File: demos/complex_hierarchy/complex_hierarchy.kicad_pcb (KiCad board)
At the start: 2 copper layers, 100.7 x 80 mm, 68 parts, among them P1 CONN_2, P2 CONN_2, P3 CONN_2, P4 CONN_2, P5 CONN_2, P6 CONN_2, Q1 MPSA92, Q2 MPSA42, Q3 MPSA92, Q4 MPSA42, Q5 MPSA92, Q6 MPSA42, Q7 MPSA92, Q8 MPSA42, U1 ICL7660, U2 78L05, U3 LM358N, U4 LM358N

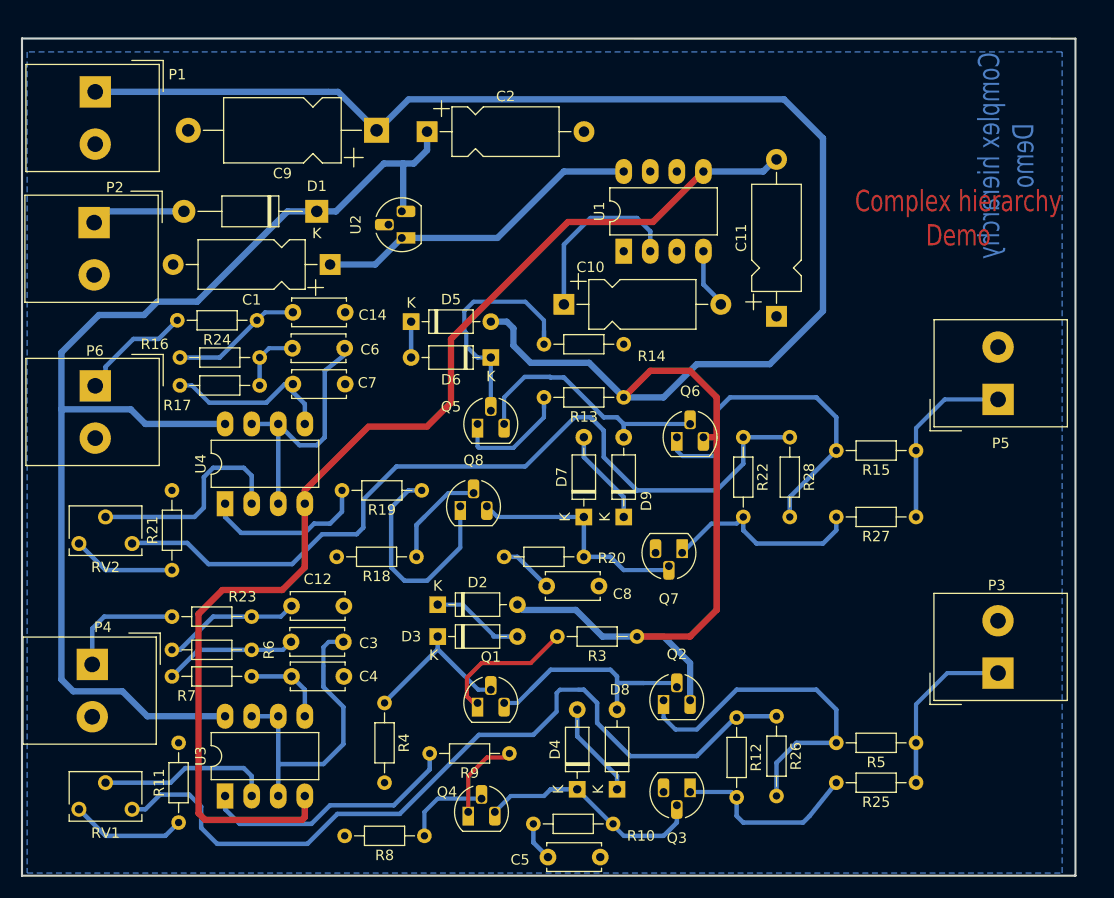
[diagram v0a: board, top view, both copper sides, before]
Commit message: feat: update kicad to 9.0.0+dfsg-1
Signed-off-by: lhdjply <lhdjply@126.com>
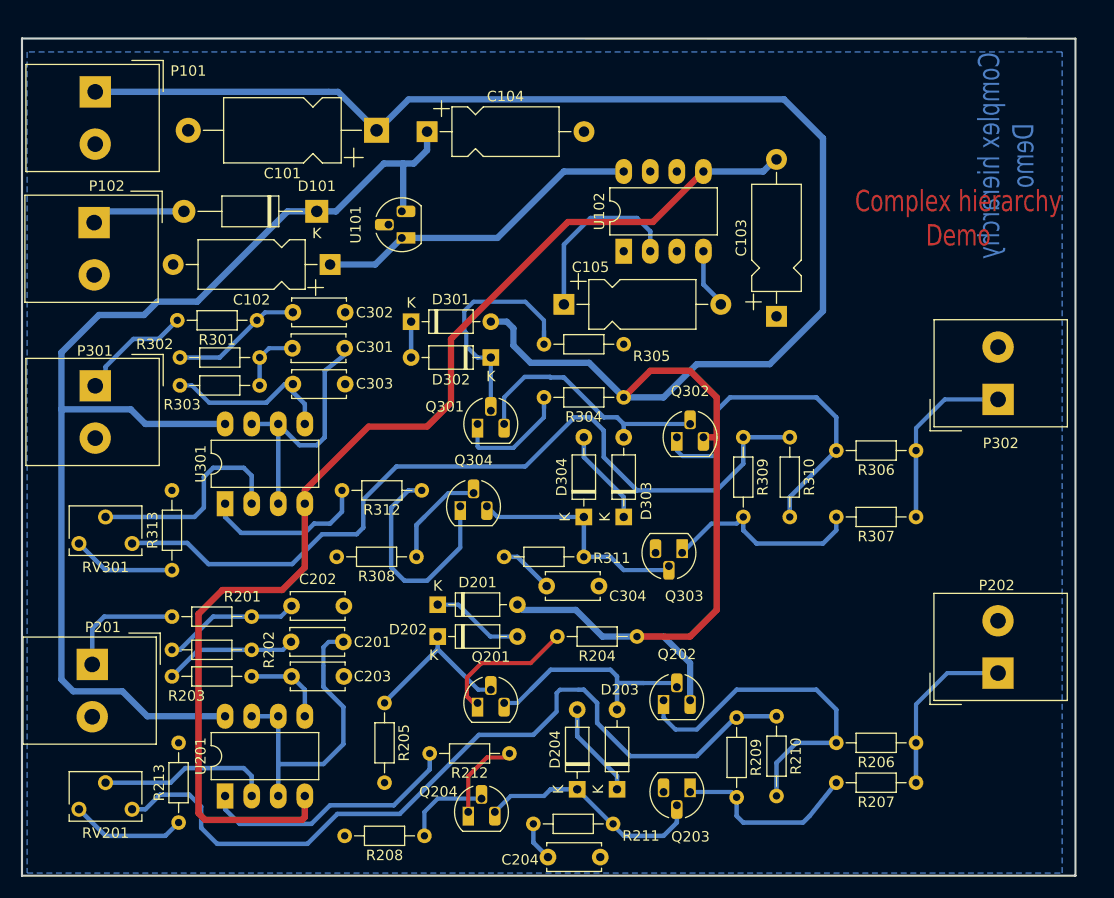
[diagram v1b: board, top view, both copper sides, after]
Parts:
- C101: renamed from C9; footprint Capacitor_THT:CP_Axial_L11.0mm_D6.0mm_P18.00mm_Horizontal -> complex_hierarchy:CP_Axial_L11.0mm_D6.0mm_P18.00mm_Horizontal
- C102: renamed from C1; footprint Capacitor_THT:CP_Axial_L10.0mm_D4.5mm_P15.00mm_Horizontal -> complex_hierarchy:CP_Axial_L10.0mm_D4.5mm_P15.00mm_Horizontal
- C103: renamed from C11; footprint Capacitor_THT:CP_Axial_L10.0mm_D4.5mm_P15.00mm_Horizontal -> complex_hierarchy:CP_Axial_L10.0mm_D4.5mm_P15.00mm_Horizontal
- C104: renamed from C2; footprint Capacitor_THT:CP_Axial_L10.0mm_D4.5mm_P15.00mm_Horizontal -> complex_hierarchy:CP_Axial_L10.0mm_D4.5mm_P15.00mm_Horizontal
- C105: renamed from C10; footprint Capacitor_THT:CP_Axial_L10.0mm_D4.5mm_P15.00mm_Horizontal -> complex_hierarchy:CP_Axial_L10.0mm_D4.5mm_P15.00mm_Horizontal
- C201: renamed from C3; footprint Capacitor_THT:C_Disc_D5.0mm_W2.5mm_P5.00mm -> complex_hierarchy:C_Disc_D5.0mm_W2.5mm_P5.00mm
- C202: renamed from C12; footprint Capacitor_THT:C_Disc_D5.0mm_W2.5mm_P5.00mm -> complex_hierarchy:C_Disc_D5.0mm_W2.5mm_P5.00mm
- C203: renamed from C4; footprint Capacitor_THT:C_Disc_D5.0mm_W2.5mm_P5.00mm -> complex_hierarchy:C_Disc_D5.0mm_W2.5mm_P5.00mm
- C204: renamed from C5; footprint Capacitor_THT:C_Disc_D5.0mm_W2.5mm_P5.00mm -> complex_hierarchy:C_Disc_D5.0mm_W2.5mm_P5.00mm
- C301: renamed from C6; footprint Capacitor_THT:C_Disc_D5.0mm_W2.5mm_P5.00mm -> complex_hierarchy:C_Disc_D5.0mm_W2.5mm_P5.00mm
- C302: renamed from C14; footprint Capacitor_THT:C_Disc_D5.0mm_W2.5mm_P5.00mm -> complex_hierarchy:C_Disc_D5.0mm_W2.5mm_P5.00mm
- C303: renamed from C7; footprint Capacitor_THT:C_Disc_D5.0mm_W2.5mm_P5.00mm -> complex_hierarchy:C_Disc_D5.0mm_W2.5mm_P5.00mm
- C304: renamed from C8; footprint Capacitor_THT:C_Disc_D5.0mm_W2.5mm_P5.00mm -> complex_hierarchy:C_Disc_D5.0mm_W2.5mm_P5.00mm
- D101: renamed from D1; footprint Diode_THT:D_DO-41_SOD81_P12.70mm_Horizontal -> complex_hierarchy:D_DO-41_SOD81_P12.70mm_Horizontal
- D201: renamed from D2; footprint Diode_THT:D_DO-35_SOD27_P7.62mm_Horizontal -> complex_hierarchy:D_DO-35_SOD27_P7.62mm_Horizontal
- D202: renamed from D3; footprint Diode_THT:D_DO-35_SOD27_P7.62mm_Horizontal -> complex_hierarchy:D_DO-35_SOD27_P7.62mm_Horizontal
- D203: renamed from D8; footprint Diode_THT:D_DO-35_SOD27_P7.62mm_Horizontal -> complex_hierarchy:D_DO-35_SOD27_P7.62mm_Horizontal
- D204: renamed from D4; footprint Diode_THT:D_DO-35_SOD27_P7.62mm_Horizontal -> complex_hierarchy:D_DO-35_SOD27_P7.62mm_Horizontal
- D301: renamed from D5; footprint Diode_THT:D_DO-35_SOD27_P7.62mm_Horizontal -> complex_hierarchy:D_DO-35_SOD27_P7.62mm_Horizontal
- D302: renamed from D6; footprint Diode_THT:D_DO-35_SOD27_P7.62mm_Horizontal -> complex_hierarchy:D_DO-35_SOD27_P7.62mm_Horizontal
- D303: renamed from D9; footprint Diode_THT:D_DO-35_SOD27_P7.62mm_Horizontal -> complex_hierarchy:D_DO-35_SOD27_P7.62mm_Horizontal
- D304: renamed from D7; footprint Diode_THT:D_DO-35_SOD27_P7.62mm_Horizontal -> complex_hierarchy:D_DO-35_SOD27_P7.62mm_Horizontal
- P101: renamed from P1; footprint TerminalBlock_Altech:Altech_AK300_1x02_P5.00mm_45-Degree -> complex_hierarchy:Altech_AK300_1x02_P5.00mm_45-Degree
- P102: renamed from P2; footprint TerminalBlock_Altech:Altech_AK300_1x02_P5.00mm_45-Degree -> complex_hierarchy:Altech_AK300_1x02_P5.00mm_45-Degree
- P201: renamed from P4; footprint TerminalBlock_Altech:Altech_AK300_1x02_P5.00mm_45-Degree -> complex_hierarchy:Altech_AK300_1x02_P5.00mm_45-Degree
- P202: renamed from P3; footprint TerminalBlock_Altech:Altech_AK300_1x02_P5.00mm_45-Degree -> complex_hierarchy:Altech_AK300_1x02_P5.00mm_45-Degree
- P301: renamed from P6; footprint TerminalBlock_Altech:Altech_AK300_1x02_P5.00mm_45-Degree -> complex_hierarchy:Altech_AK300_1x02_P5.00mm_45-Degree
- P302: renamed from P5; footprint TerminalBlock_Altech:Altech_AK300_1x02_P5.00mm_45-Degree -> complex_hierarchy:Altech_AK300_1x02_P5.00mm_45-Degree
- Q201: renamed from Q1; footprint Package_TO_SOT_THT:TO-92_HandSolder -> complex_hierarchy:TO-92_HandSolder
- Q202: renamed from Q2; footprint Package_TO_SOT_THT:TO-92_HandSolder -> complex_hierarchy:TO-92_HandSolder
- Q203: renamed from Q3; footprint Package_TO_SOT_THT:TO-92_HandSolder -> complex_hierarchy:TO-92_HandSolder
- Q204: renamed from Q4; footprint Package_TO_SOT_THT:TO-92_HandSolder -> complex_hierarchy:TO-92_HandSolder
- Q301: renamed from Q5; footprint Package_TO_SOT_THT:TO-92_HandSolder -> complex_hierarchy:TO-92_HandSolder
- Q302: renamed from Q6; footprint Package_TO_SOT_THT:TO-92_HandSolder -> complex_hierarchy:TO-92_HandSolder
- Q303: renamed from Q7; footprint Package_TO_SOT_THT:TO-92_HandSolder -> complex_hierarchy:TO-92_HandSolder
- Q304: renamed from Q8; footprint Package_TO_SOT_THT:TO-92_HandSolder -> complex_hierarchy:TO-92_HandSolder
- R201: renamed from R23; footprint Resistor_THT:R_Axial_DIN0204_L3.6mm_D1.6mm_P7.62mm_Horizontal -> complex_hierarchy:R_Axial_DIN0204_L3.6mm_D1.6mm_P7.62mm_Horizontal
- R202: renamed from R6; footprint Resistor_THT:R_Axial_DIN0204_L3.6mm_D1.6mm_P7.62mm_Horizontal -> complex_hierarchy:R_Axial_DIN0204_L3.6mm_D1.6mm_P7.62mm_Horizontal
- R203: renamed from R7; footprint Resistor_THT:R_Axial_DIN0204_L3.6mm_D1.6mm_P7.62mm_Horizontal -> complex_hierarchy:R_Axial_DIN0204_L3.6mm_D1.6mm_P7.62mm_Horizontal
- R204: renamed from R3; footprint Resistor_THT:R_Axial_DIN0204_L3.6mm_D1.6mm_P7.62mm_Horizontal -> complex_hierarchy:R_Axial_DIN0204_L3.6mm_D1.6mm_P7.62mm_Horizontal
- R205: renamed from R4; footprint Resistor_THT:R_Axial_DIN0204_L3.6mm_D1.6mm_P7.62mm_Horizontal -> complex_hierarchy:R_Axial_DIN0204_L3.6mm_D1.6mm_P7.62mm_Horizontal
- R206: renamed from R5; footprint Resistor_THT:R_Axial_DIN0204_L3.6mm_D1.6mm_P7.62mm_Horizontal -> complex_hierarchy:R_Axial_DIN0204_L3.6mm_D1.6mm_P7.62mm_Horizontal
- R207: renamed from R25; footprint Resistor_THT:R_Axial_DIN0204_L3.6mm_D1.6mm_P7.62mm_Horizontal -> complex_hierarchy:R_Axial_DIN0204_L3.6mm_D1.6mm_P7.62mm_Horizontal
- R208: renamed from R8; footprint Resistor_THT:R_Axial_DIN0204_L3.6mm_D1.6mm_P7.62mm_Horizontal -> complex_hierarchy:R_Axial_DIN0204_L3.6mm_D1.6mm_P7.62mm_Horizontal
- R209: renamed from R12; footprint Resistor_THT:R_Axial_DIN0204_L3.6mm_D1.6mm_P7.62mm_Horizontal -> complex_hierarchy:R_Axial_DIN0204_L3.6mm_D1.6mm_P7.62mm_Horizontal
- R210: renamed from R26; footprint Resistor_THT:R_Axial_DIN0204_L3.6mm_D1.6mm_P7.62mm_Horizontal -> complex_hierarchy:R_Axial_DIN0204_L3.6mm_D1.6mm_P7.62mm_Horizontal
- R211: renamed from R10; footprint Resistor_THT:R_Axial_DIN0204_L3.6mm_D1.6mm_P7.62mm_Horizontal -> complex_hierarchy:R_Axial_DIN0204_L3.6mm_D1.6mm_P7.62mm_Horizontal
- R212: renamed from R9; footprint Resistor_THT:R_Axial_DIN0204_L3.6mm_D1.6mm_P7.62mm_Horizontal -> complex_hierarchy:R_Axial_DIN0204_L3.6mm_D1.6mm_P7.62mm_Horizontal
- R213: renamed from R11; footprint Resistor_THT:R_Axial_DIN0204_L3.6mm_D1.6mm_P7.62mm_Horizontal -> complex_hierarchy:R_Axial_DIN0204_L3.6mm_D1.6mm_P7.62mm_Horizontal
- R301: renamed from R24; footprint Resistor_THT:R_Axial_DIN0204_L3.6mm_D1.6mm_P7.62mm_Horizontal -> complex_hierarchy:R_Axial_DIN0204_L3.6mm_D1.6mm_P7.62mm_Horizontal
- R302: renamed from R16; footprint Resistor_THT:R_Axial_DIN0204_L3.6mm_D1.6mm_P7.62mm_Horizontal -> complex_hierarchy:R_Axial_DIN0204_L3.6mm_D1.6mm_P7.62mm_Horizontal
- R303: renamed from R17; footprint Resistor_THT:R_Axial_DIN0204_L3.6mm_D1.6mm_P7.62mm_Horizontal -> complex_hierarchy:R_Axial_DIN0204_L3.6mm_D1.6mm_P7.62mm_Horizontal
- R304: renamed from R13; footprint Resistor_THT:R_Axial_DIN0204_L3.6mm_D1.6mm_P7.62mm_Horizontal -> complex_hierarchy:R_Axial_DIN0204_L3.6mm_D1.6mm_P7.62mm_Horizontal
- R305: renamed from R14; footprint Resistor_THT:R_Axial_DIN0204_L3.6mm_D1.6mm_P7.62mm_Horizontal -> complex_hierarchy:R_Axial_DIN0204_L3.6mm_D1.6mm_P7.62mm_Horizontal
- R306: renamed from R15; footprint Resistor_THT:R_Axial_DIN0204_L3.6mm_D1.6mm_P7.62mm_Horizontal -> complex_hierarchy:R_Axial_DIN0204_L3.6mm_D1.6mm_P7.62mm_Horizontal
- R307: renamed from R27; footprint Resistor_THT:R_Axial_DIN0204_L3.6mm_D1.6mm_P7.62mm_Horizontal -> complex_hierarchy:R_Axial_DIN0204_L3.6mm_D1.6mm_P7.62mm_Horizontal
- R308: renamed from R18; footprint Resistor_THT:R_Axial_DIN0204_L3.6mm_D1.6mm_P7.62mm_Horizontal -> complex_hierarchy:R_Axial_DIN0204_L3.6mm_D1.6mm_P7.62mm_Horizontal
- R309: renamed from R22; footprint Resistor_THT:R_Axial_DIN0204_L3.6mm_D1.6mm_P7.62mm_Horizontal -> complex_hierarchy:R_Axial_DIN0204_L3.6mm_D1.6mm_P7.62mm_Horizontal
- R310: renamed from R28; footprint Resistor_THT:R_Axial_DIN0204_L3.6mm_D1.6mm_P7.62mm_Horizontal -> complex_hierarchy:R_Axial_DIN0204_L3.6mm_D1.6mm_P7.62mm_Horizontal
- R311: renamed from R20; footprint Resistor_THT:R_Axial_DIN0204_L3.6mm_D1.6mm_P7.62mm_Horizontal -> complex_hierarchy:R_Axial_DIN0204_L3.6mm_D1.6mm_P7.62mm_Horizontal
- R312: renamed from R19; footprint Resistor_THT:R_Axial_DIN0204_L3.6mm_D1.6mm_P7.62mm_Horizontal -> complex_hierarchy:R_Axial_DIN0204_L3.6mm_D1.6mm_P7.62mm_Horizontal
- R313: renamed from R21; footprint Resistor_THT:R_Axial_DIN0204_L3.6mm_D1.6mm_P7.62mm_Horizontal -> complex_hierarchy:R_Axial_DIN0204_L3.6mm_D1.6mm_P7.62mm_Horizontal
- RV201: renamed from RV1; footprint Potentiometer_THT:Potentiometer_Bourns_3266W_Vertical -> complex_hierarchy:Potentiometer_Bourns_3266W_Vertical
- RV301: renamed from RV2; footprint Potentiometer_THT:Potentiometer_Bourns_3266W_Vertical -> complex_hierarchy:Potentiometer_Bourns_3266W_Vertical
- U101: renamed from U2; footprint Package_TO_SOT_THT:TO-92_HandSolder -> complex_hierarchy:TO-92_HandSolder
- U102: renamed from U1; footprint Package_DIP:DIP-8_W7.62mm_LongPads -> complex_hierarchy:DIP-8_W7.62mm_LongPads
- U201: renamed from U3; footprint Package_DIP:DIP-8_W7.62mm_LongPads -> complex_hierarchy:DIP-8_W7.62mm_LongPads
- U301: renamed from U4; footprint Package_DIP:DIP-8_W7.62mm_LongPads -> complex_hierarchy:DIP-8_W7.62mm_LongPads
